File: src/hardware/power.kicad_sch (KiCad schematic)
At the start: 0 parts

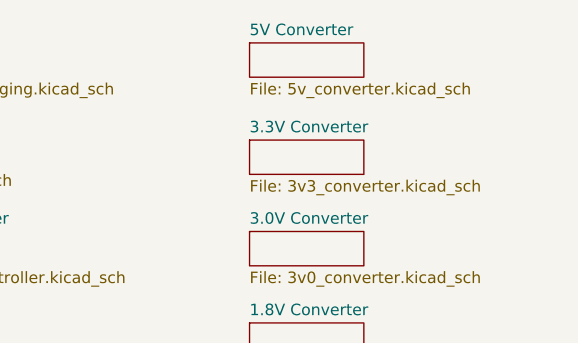
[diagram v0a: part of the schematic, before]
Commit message: Changed 5V net to 4.5V net
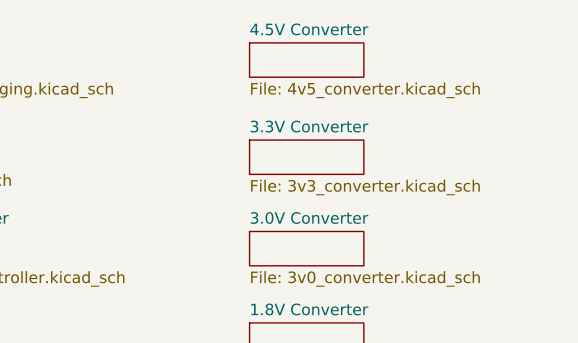
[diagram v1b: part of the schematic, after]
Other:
- sheet 5V Converter renamed 4.5V Converter
- sheet 4.5V Converter: file 5v_converter.kicad_sch -> 4v5_converter.kicad_sch
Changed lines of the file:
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@@
 			(color 0 0 0 0.0000)
 		)
-		(property "Sheetname" "5V Converter"
+		(property "Sheetname" "4.5V Converter"
 			(at 83.82 57.0734 0)
 			(effects
@@
 			)
 		)
-		(property "Sheetfile" "5v_converter.kicad_sch"
+		(property "Sheetfile" "4v5_converter.kicad_sch"
 			(at 83.82 62.1796 0)
 			(effects

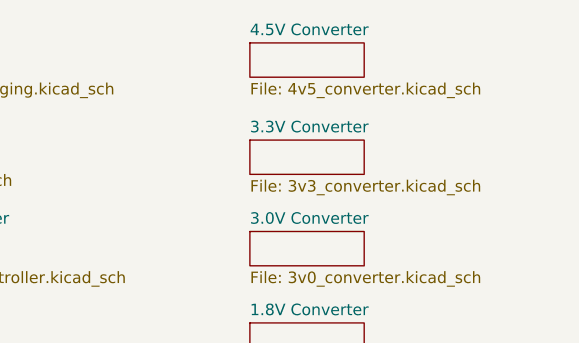
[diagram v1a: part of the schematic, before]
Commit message: Removed 4.5V page. 4.5V will come from the charging controller directly
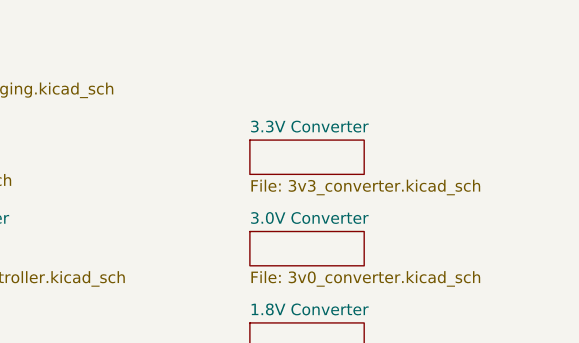
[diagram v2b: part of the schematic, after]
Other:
- removed sheet 4.5V Converter
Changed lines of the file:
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@@
-		)
-	)
-	(sheet
-		(at 83.82 57.785)
-		(size 12.7 3.81)
-		(exclude_from_sim no)
-		(in_bom yes)
-		(on_board yes)
-		(dnp no)
-		(fields_autoplaced yes)
-		(stroke
-			(width 0.1524)
-			(type solid)
-		)
-		(fill
-			(color 0 0 0 0.0000)
-		)
-		(property "Sheetname" "4.5V Converter"
-			(at 83.82 57.0734 0)
-			(effects
-				(font
-					(size 1.27 1.27)
-				)
-				(justify left bottom)
-			)
-		)
-		(property "Sheetfile" "4v5_converter.kicad_sch"
-			(at 83.82 62.1796 0)
-			(effects
-				(font
-					(size 1.27 1.27)
-				)
-				(justify left top)
-			)
-		)
-		(instances
-			(project "raywatch"
-				(path "/7b654ee8-2a53-4d39-8b7d-32c7bb3cb0ed/6e6a70ea-4db2-4b59-a2d7-c468f9b8b5a6"
-					(page "18")
-				)
-			)
 		)
 	)

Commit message: Created Power Diagram
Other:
- note added: "+1V8"
- note added: "+3V0"
- note added: "+3V3"
- note added: "+4V5"
- note added: "+BATT"
- note added: "-BATT"
- note added: "Battery"
- note added: "GND"
- note added: "VBAT"
- note added: "VIN"
- note added: "VSOLAR"
- note added: "VSYS"
- note added: "Wireless Charging Coil"

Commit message: Added battery
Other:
- added sheet Battery (battery.kicad_sch)
- note removed: "Battery"
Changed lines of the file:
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@@
 		(date "2026-10-21")
 	)
-	(rectangle
-		(start 116.332 145.542)
-		(end 119.888 154.432)
-		(stroke
-			(width 0)
-			(type default)
-		)
-		(fill
-			(type none)
-		)
-	)
 	(text "+3V0"
 		(exclude_from_sim no)
@@
 		)
 	)
-	(text "Battery"
-		(exclude_from_sim no)
-		(at 123.444 150.368 0)
-		(effects
-			(font
-				(size 1.27 1.27)
-			)
-		)
-	)
 	(text "VBAT"
 		(exclude_from_sim no)
@@
 	(text "-BATT"
 		(exclude_from_sim no)
-		(at 114.046 143.256 0)
+		(at 114.046 143.764 0)
 		(effects
 			(font
@@
 	(text "+BATT"
 		(exclude_from_sim no)
-		(at 121.92 143.256 0)
+		(at 121.92 143.764 0)
 		(effects
 			(font
@@
 	(polyline
 		(pts
+			(xy 117.348 145.542) (xy 117.348 146.304)
+		)
+		(stroke
+			(width 0)
+			(type default)
+		)
+	)
+	(polyline
+		(pts
 			(xy 117.348 129.54) (xy 107.95 129.54)
 		)
@@
 		(pts
 			(xy 124.714 99.822) (xy 162.306 99.822)
+		)
+		(stroke
+			(width 0)
+			(type default)
+		)
+	)
+	(polyline
+		(pts
+			(xy 118.872 145.542) (xy 118.872 146.304)
 		)
 		(stroke
@@
 				)
 			)
+		)
+	)
+	(sheet
+		(at 116.205 148.717)
+		(size 3.81 12.7)
+		(exclude_from_sim no)
+		(in_bom yes)
+		(on_board yes)
+		(dnp no)
+		(fields_autoplaced yes)
+		(stroke
+			(width 0.1524)
+			(type solid)
+		)
+		(fill
+			(color 0 0 0 0.0000)
+		)
+		(property "Sheetname" "Battery"
+			(at 116.205 148.0054 0)
+			(effects
+				(font
+					(size 1.27 1.27)
+				)
+				(justify left bottom)
+			)
+		)
+		(property "Sheetfile" "battery.kicad_sch"
+			(at 116.205 162.0016 0)
+			(effects
+				(font
+					(size 1.27 1.27)
+				)
+				(justify left top)
+			)
+		)
+		(instances
+			(project "raywatch"
+				(path "/7b654ee8-2a53-4d39-8b7d-32c7bb3cb0ed/6e6a70ea-4db2-4b59-a2d7-c468f9b8b5a6"
+					(page "24")
+				)
+			)
